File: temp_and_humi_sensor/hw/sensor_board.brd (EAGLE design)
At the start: 63.5 x 52.1 mm, 13 parts, among them U1 328P

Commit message: Fixed power lines
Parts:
- added C3: 0.1uF, SparkFun-Capacitors:CAP-PTH-SMALL-KIT
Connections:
- net GND: now also C3.1
- net VCC: now also C3.2
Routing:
- net VCC: track 93.0 -> 122.1 mm
- net MOSI: track 15.3 -> 29.8 mm
- net MISO: track 28.8 -> 34.9 mm
- added copper zone on layer 16, net N$5
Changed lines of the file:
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@@
 </element>
 <element name="J2" library="SparkFun-Connectors" package="1X02" value="" x="16.51" y="13.97"/>
+<element name="C3" library="SparkFun-Capacitors" package="CAP-PTH-SMALL-KIT" value="0.1uF" x="16.51" y="44.45" rot="R90">
+<attribute name="PROD_ID" value="CAP-08370" x="16.51" y="44.45" size="1.778" layer="27" rot="R90" display="off"/>
+</element>
 </elements>
 <signals>
@@
 <contactref element="U1" pad="7"/>
 <contactref element="U2" pad="VDD"/>
-<contactref element="R2" pad="P$2"/>
-<wire x1="45.72" y1="36.83" x2="55.88" y2="36.83" width="0.6096" layer="16"/>
 <wire x1="10.16" y1="25.4" x2="10.287" y2="29.21" width="0.6096" layer="16"/>
 <wire x1="34.29" y1="25.4" x2="34.29" y2="26.797" width="0.6096" layer="16"/>
@@
 <wire x1="10.287" y1="29.21" x2="10.287" y2="35.413" width="0.6096" layer="16"/>
 <wire x1="10.287" y1="35.413" x2="10.14" y2="35.56" width="0.4064" layer="16"/>
-<wire x1="55.88" y1="36.83" x2="55.88" y2="33.02" width="0.6096" layer="16"/>
 <contactref element="U1" pad="20"/>
 <wire x1="34.29" y1="25.4" x2="34.29" y2="22.86" width="0.6096" layer="16"/>
@@
 <wire x1="34.29" y1="29.21" x2="34.29" y2="28.067" width="0.6096" layer="16"/>
 <wire x1="34.29" y1="28.067" x2="34.417" y2="27.94" width="0.6096" layer="16"/>
-<wire x1="33.02" y1="30.48" x2="34.29" y2="31.75" width="0.6096" layer="16"/>
-<wire x1="34.29" y1="31.75" x2="34.29" y2="34.29" width="0.6096" layer="16"/>
-<wire x1="34.29" y1="34.29" x2="36.83" y2="36.83" width="0.6096" layer="16"/>
-<wire x1="36.83" y1="36.83" x2="45.72" y2="36.83" width="0.6096" layer="16"/>
+<contactref element="R2" pad="P$2"/>
+<contactref element="C3" pad="2"/>
+<wire x1="10.16" y1="40.64" x2="10.16" y2="44.45" width="0.6096" layer="16"/>
+<wire x1="10.16" y1="44.45" x2="11.43" y2="45.72" width="0.6096" layer="16"/>
+<wire x1="11.43" y1="45.72" x2="16.383" y2="45.72" width="0.6096" layer="16"/>
+<wire x1="16.383" y1="45.72" x2="16.51" y2="45.847" width="0.6096" layer="16"/>
+<wire x1="16.51" y1="45.847" x2="36.703" y2="45.847" width="0.6096" layer="16"/>
+<wire x1="36.703" y1="45.847" x2="39.37" y2="43.18" width="0.6096" layer="16"/>
+<wire x1="39.37" y1="43.18" x2="39.37" y2="39.37" width="0.6096" layer="16"/>
+<wire x1="39.37" y1="39.37" x2="41.91" y2="36.83" width="0.6096" layer="16"/>
+<wire x1="41.91" y1="36.83" x2="45.72" y2="36.83" width="0.6096" layer="16"/>
+<wire x1="45.72" y1="36.83" x2="55.88" y2="36.83" width="0.6096" layer="16"/>
+<wire x1="55.88" y1="36.83" x2="55.88" y2="33.02" width="0.6096" layer="16"/>
 </signal>
 <signal name="GND">
@@
 <wire x1="7.64" y1="35.56" x2="7.64" y2="29.357" width="0.4064" layer="16"/>
 <wire x1="7.64" y1="29.357" x2="7.493" y2="29.21" width="0.4064" layer="16"/>
-<polygon width="0.254" layer="16" isolate="0.3048">
+<polygon width="0.254" layer="16" isolate="0.6096">
 <vertex x="0" y="52.07"/>
 <vertex x="63.5" y="52.07"/>
@@
 </polygon>
 <contactref element="J2" pad="2"/>
+<contactref element="C3" pad="1"/>
+<wire x1="34.29" y1="17.78" x2="31.75" y2="25.4" width="0" layer="19" extent="1-1"/>
+<wire x1="16.51" y1="43.053" x2="7.62" y2="40.64" width="0" layer="19" extent="1-1"/>
 </signal>
 <signal name="MOSI">
 <contactref element="U1" pad="17"/>
 <contactref element="J1" pad="6"/>
-<wire x1="10.16" y1="20.32" x2="12.7" y2="22.86" width="0.4064" layer="16"/>
-<wire x1="12.7" y1="22.86" x2="17.78" y2="22.86" width="0.4064" layer="16"/>
-<wire x1="17.78" y1="22.86" x2="21.59" y2="19.05" width="0.4064" layer="16"/>
-<wire x1="21.59" y1="19.05" x2="21.59" y2="17.78" width="0.4064" layer="16"/>
+<wire x1="10.16" y1="20.32" x2="11.43" y2="20.32" width="0.4064" layer="16"/>
+<wire x1="11.43" y1="20.32" x2="12.7" y2="19.05" width="0.4064" layer="16"/>
+<wire x1="12.7" y1="19.05" x2="12.7" y2="11.43" width="0.4064" layer="16"/>
+<wire x1="12.7" y1="11.43" x2="13.97" y2="10.16" width="0.4064" layer="16"/>
+<wire x1="13.97" y1="10.16" x2="21.59" y2="10.16" width="0.4064" layer="16"/>
+<wire x1="21.59" y1="10.16" x2="24.13" y2="12.7" width="0.4064" layer="16"/>
+<wire x1="24.13" y1="12.7" x2="24.13" y2="15.24" width="0.4064" layer="16"/>
+<wire x1="24.13" y1="15.24" x2="21.59" y2="17.78" width="0.4064" layer="16"/>
 </signal>
 <signal name="MISO">
 <contactref element="U1" pad="18"/>
 <contactref element="J1" pad="7"/>
-<wire x1="7.62" y1="17.78" x2="7.62" y2="12.7" width="0.4064" layer="16"/>
-<wire x1="7.62" y1="12.7" x2="10.16" y2="10.16" width="0.4064" layer="16"/>
-<wire x1="10.16" y1="10.16" x2="21.59" y2="10.16" width="0.4064" layer="16"/>
-<wire x1="21.59" y1="10.16" x2="24.13" y2="12.7" width="0.4064" layer="16"/>
-<wire x1="24.13" y1="12.7" x2="24.13" y2="17.78" width="0.4064" layer="16"/>
+<wire x1="7.62" y1="17.78" x2="6.35" y2="16.51" width="0.4064" layer="16"/>
+<wire x1="6.35" y1="16.51" x2="6.35" y2="11.43" width="0.4064" layer="16"/>
+<wire x1="6.35" y1="11.43" x2="8.89" y2="8.89" width="0.4064" layer="16"/>
+<wire x1="8.89" y1="8.89" x2="22.86" y2="8.89" width="0.4064" layer="16"/>
+<wire x1="22.86" y1="8.89" x2="25.4" y2="11.43" width="0.4064" layer="16"/>
+<wire x1="25.4" y1="11.43" x2="25.4" y2="16.51" width="0.4064" layer="16"/>
+<wire x1="25.4" y1="16.51" x2="24.13" y2="17.78" width="0.4064" layer="16"/>
 </signal>
 <signal name="SCK">
@@
 <wire x1="16.51" y1="13.97" x2="16.51" y2="17.78" width="0.4064" layer="16"/>
 </signal>
+<signal name="N$5">
+<polygon width="0" layer="16" pour="cutout">
+<vertex x="59.69" y="22.86"/>
+<vertex x="63.5" y="22.86"/>
+<vertex x="63.5" y="21.59"/>
+<vertex x="59.69" y="21.59"/>
+</polygon>
+</signal>
 </signals>

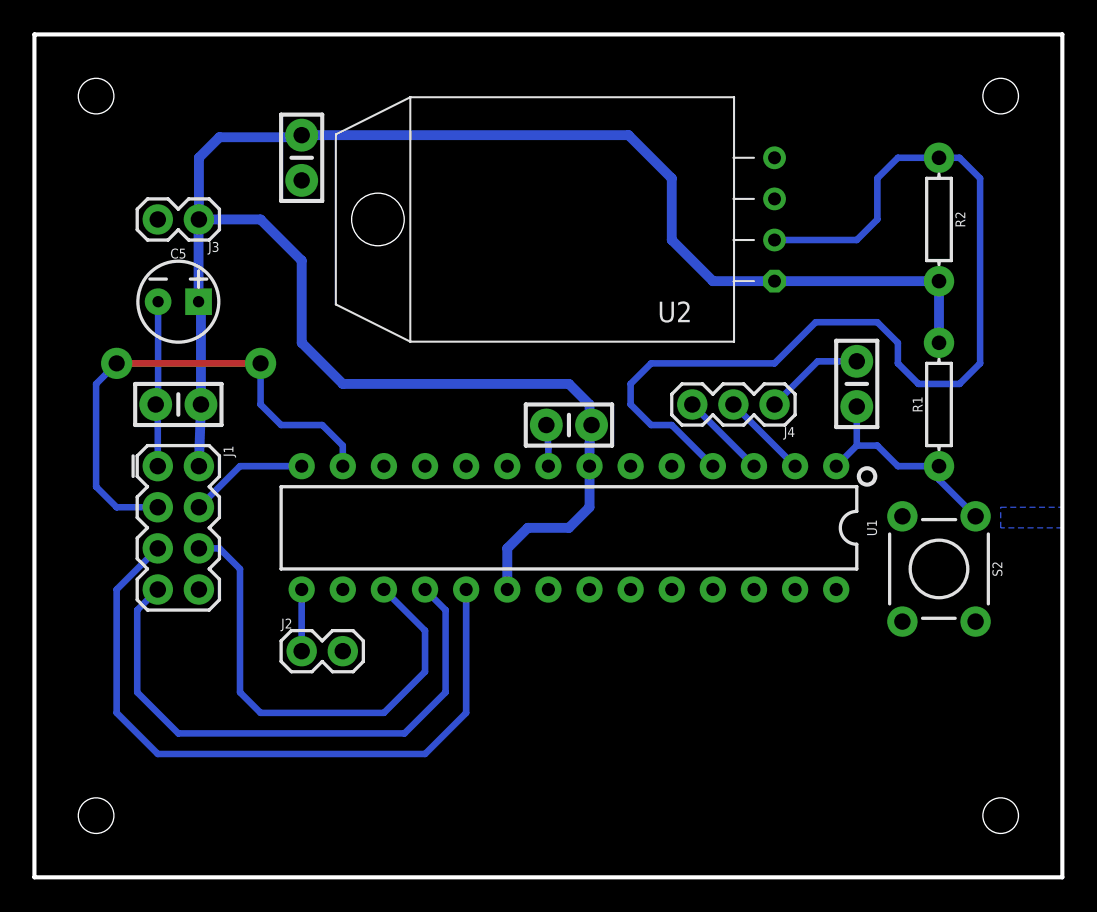
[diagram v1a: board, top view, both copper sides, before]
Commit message: Added bigger capacitor
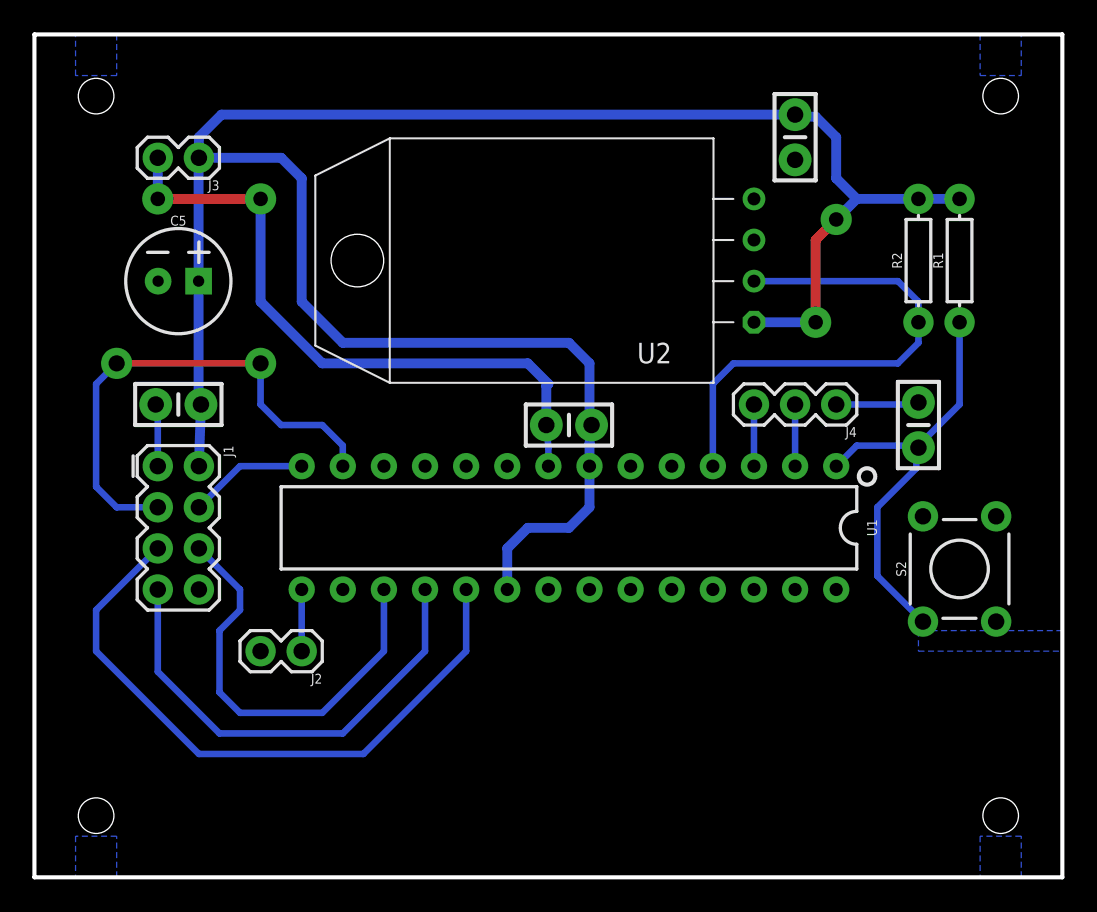
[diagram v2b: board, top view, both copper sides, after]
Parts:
- C5: value 10uF -> 100uF; device SparkFun-Capacitors:CPOL-RADIAL-2.5MM-5MM -> SparkFun-Capacitors:CPOL-RADIAL-2.5MM-6.5MM
- moved C3 30.5 mm to (47.0, 45.7)
- moved R1 8.98 mm to (57.1, 38.1)
- moved C2 4.58 mm to (54.6, 27.9)
- moved J3 3.81 mm to (10.2, 44.5)
- moved J4 3.81 mm to (49.5, 29.2)
- moved R2 2.84 mm to (54.6, 38.1), turned to 90 degrees
- moved U2 2.84 mm to (44.5, 38.1)
- moved C5 1.27 mm to (8.89, 36.8)
- moved S2 1.27 mm to (57.1, 19.1), turned to 90 degrees
- turned J2 to 180 degrees
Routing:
- net GND: track 12.8 -> 44.3 mm, vias 0 -> 2
- net N$4: track 62.2 -> 32.1 mm
- net RESET: track 13.9 -> 27.5 mm
- net VCC: track 122.1 -> 135.6 mm, vias 0 -> 2
- net MISO: track 34.9 -> 29.1 mm
- net MOSI: track 29.8 -> 26.5 mm
- net SCK: track 42.5 -> 39.9 mm
- net TX: track 5.39 -> 3.81 mm
- net RX: track 5.39 -> 3.81 mm
- net DTR: track 6.18 -> 5.13 mm
- added copper zone on layer 16, net N$10
- added copper zone on layer 16, net N$11
- added copper zone on layer 16, net N$12
- added copper zone on layer 16, net N$9
